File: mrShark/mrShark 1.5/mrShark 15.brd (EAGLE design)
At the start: 26 x 31 mm, 78 parts, among them IC1 ATMEGA168-20MU, IC2 PCA9540BDP, IC3 TIR1000PWR, IC4 TFBS4711TR1, IC5 DRV8830DRCT, IC6 LTC2990IMS#PBF, IC7 DRV8830DRCT, IC8 LTC2990IMS#PBF, Q1 TXC - 7X-1.8432MBB-T - OSC, 1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, Q2 BC817W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

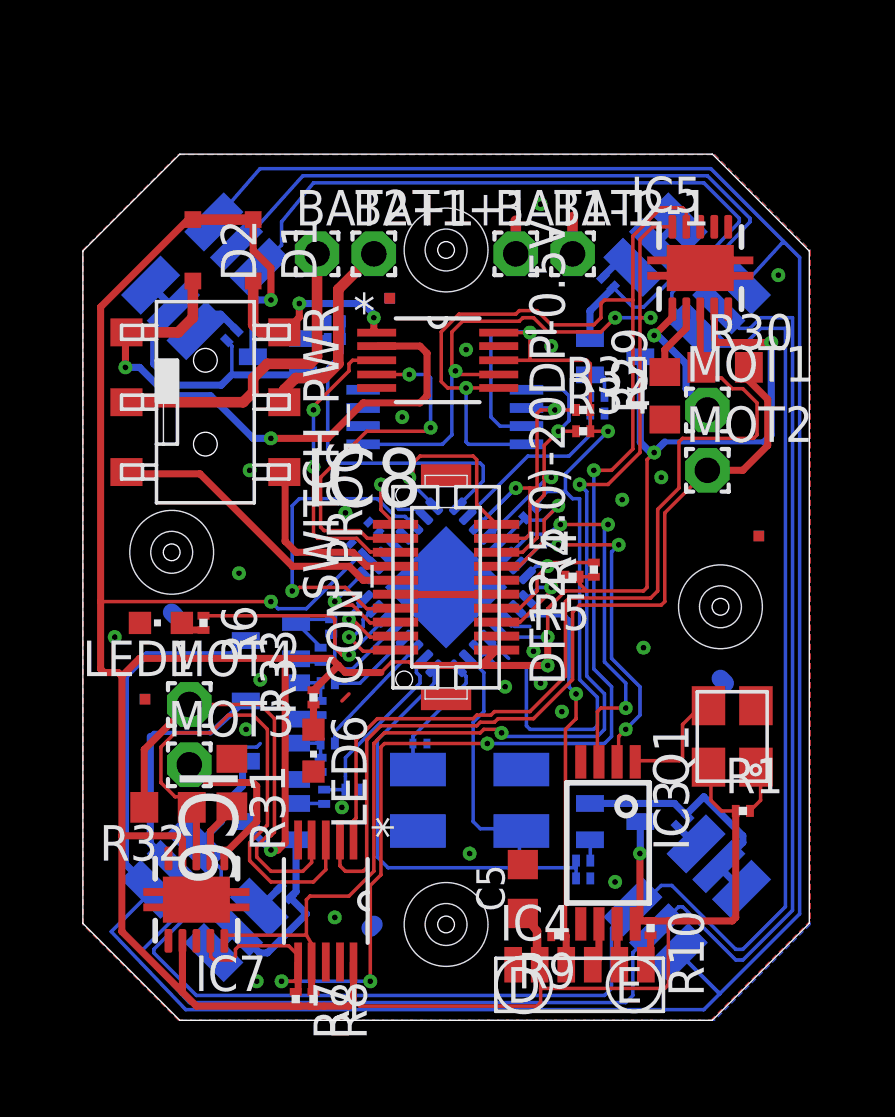
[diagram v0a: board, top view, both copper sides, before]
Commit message: Updated Board layouts an schematics
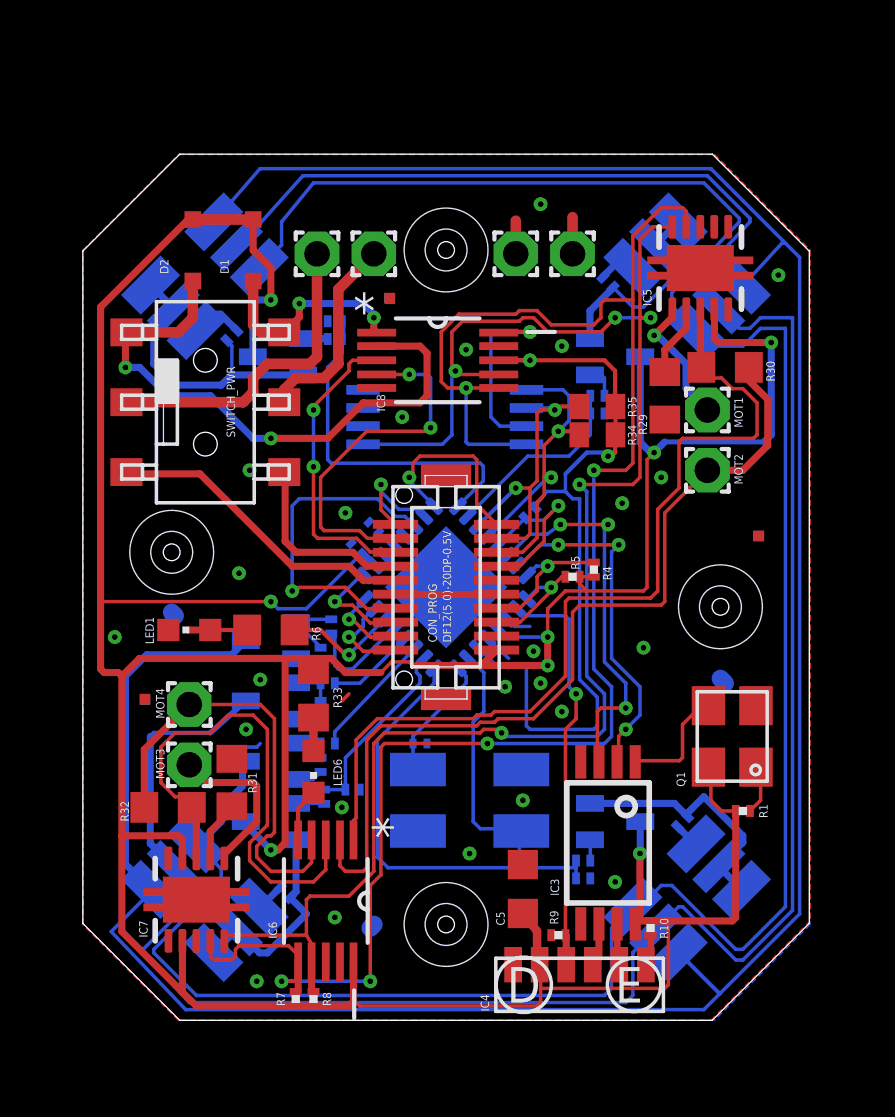
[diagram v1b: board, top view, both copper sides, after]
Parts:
- R33: value 200R -> 39R; device rcl:R0201 -> rcl:R0603
- R34, R35: device rcl:R0201 -> rcl:R0402
- R6: value 87R -> 82R; device rcl:R0201 -> rcl:R0603
- moved R6 2.43 mm to (6.73, 14.0), turned to 180 degrees
- moved LED1 1.05 mm to (3.81, 14.0)
- moved LED6 0.76 mm to (8.26, 8.89)
- moved R34 0.52 mm to (18.4, 21.0)
- moved R35 0.52 mm to (18.4, 22.0)
- moved R33 0.13 mm to (8.26, 11.7)
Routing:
- net N$3: track 8.32 -> 4.25 mm
- net GND: track 13.6 -> 15.6 mm, vias 23 -> 24
- net N$8: track 0.88 -> 2.08 mm
- net VCC: track 184.8 -> 185.4 mm, vias 10 -> 11
- net SCL: track 60.5 -> 61.0 mm
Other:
- board text added: ">"
- board text added: "FH Kiel"
- board text removed: "Fachhochschule Kiel"
